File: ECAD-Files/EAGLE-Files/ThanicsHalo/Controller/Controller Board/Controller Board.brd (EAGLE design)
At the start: 95.5 x 57.8 mm, 179 parts, among them J10 EDGE_CONNECTOR_20POS, J2 USB_A_RECEPT, J3 105450-0101, J5 EDGE_CONNECTOR_20POS, J6 MICROSD, J7 105450-0101, J8 2_PIN_CONNECTOR, J9 B2B-PH-SM4-TB(LF)(SN), Q2 2N7002P_MOSFET, T1 ALT4532M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

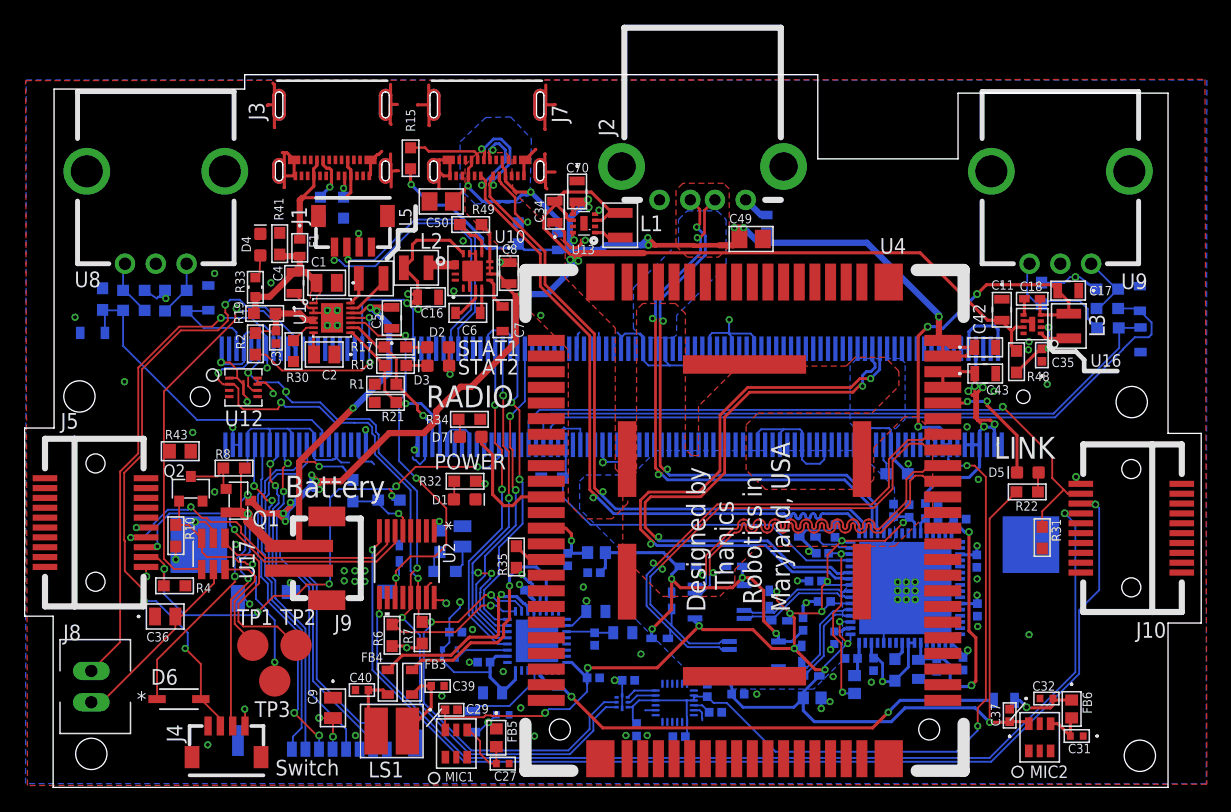
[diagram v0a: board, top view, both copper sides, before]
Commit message: Fixed USB C connector sheild pin short problem
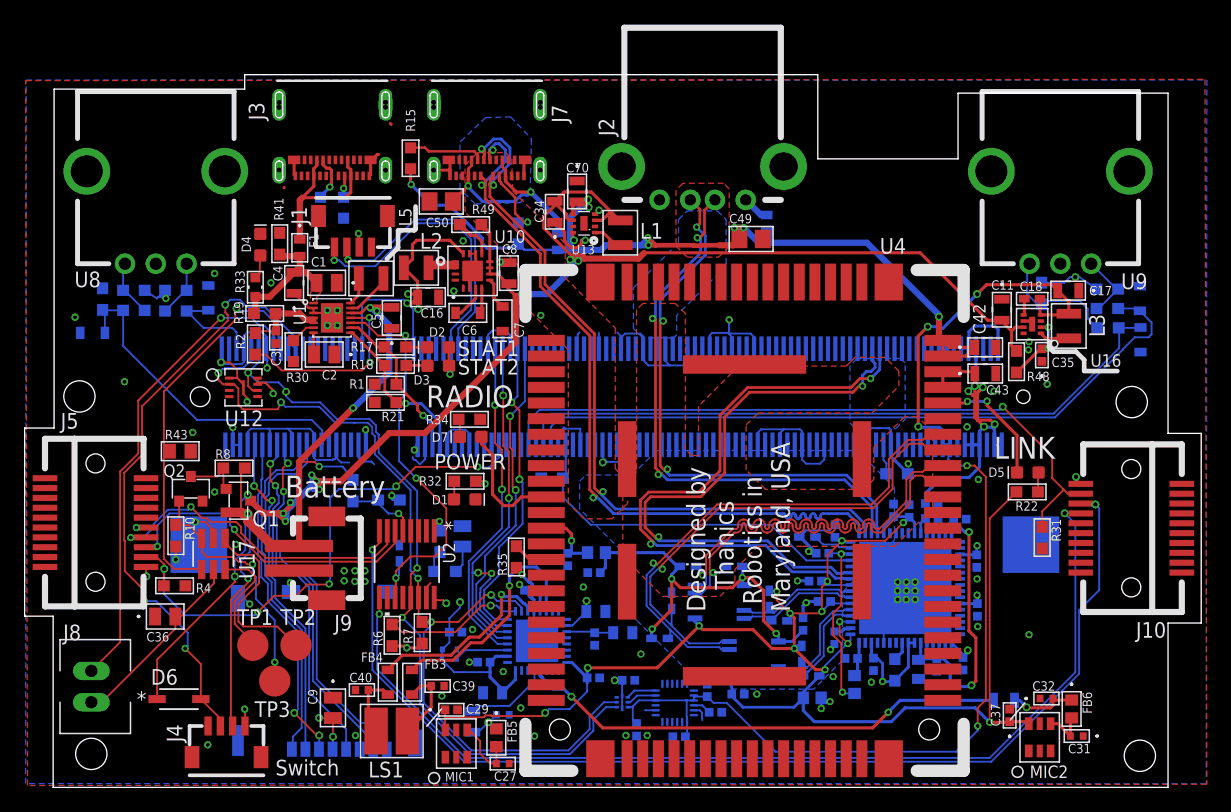
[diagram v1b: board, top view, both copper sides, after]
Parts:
- moved L1 0.61 mm to (50.2, 45.1)
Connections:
- net GND: now also J3.P$1, J3.P$2, J3.P$3, J3.P$4, J3.P$5, J3.P$6, J7.P$1, J7.P$2, J7.P$3, J7.P$4, J7.P$5, J7.P$6; no longer J3.1, J3.2, J3.3, J3.4, J7.1, J7.2, J7.3, J7.4
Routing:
- net GND: track 199.1 -> 163.9 mm
- net SWITCH_OUT: track 51.6 -> 49.8 mm
- net N$18: track 28.5 -> 26.8 mm
- net N$54: track 40.5 -> 39.0 mm
- net +3V3: track 160.9 -> 159.7 mm
- net BATT_OUTPUT: track 133.9 -> 135.1 mm
- net N$17: track 27.0 -> 26.1 mm
- net N$41: track 16.5 -> 15.7 mm
- net N$43: track 20.0 -> 19.3 mm
- added copper zone on layer 15, net +3V1
- added copper zone on layer 15, net +3V2
- added copper zone on layer 15, net +3V4
- added copper zone on layer 15, net +3V5
- added copper zone on layer 15, net +3V6
- added copper zone on layer 15, net +3V7
- added copper zone on layer 15, net +3V8
- added copper zone on layer 2, net GND3
- added copper zone on layer 2, net GND4
- added copper zone on layer 2, net GND5
- added copper zone on layer 2, net GND6
- added copper zone on layer 2, net GND7
- added copper zone on layer 2, net GND8
- added copper zone on layer 2, net GND9
